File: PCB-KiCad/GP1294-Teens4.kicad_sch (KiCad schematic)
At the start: 10 parts

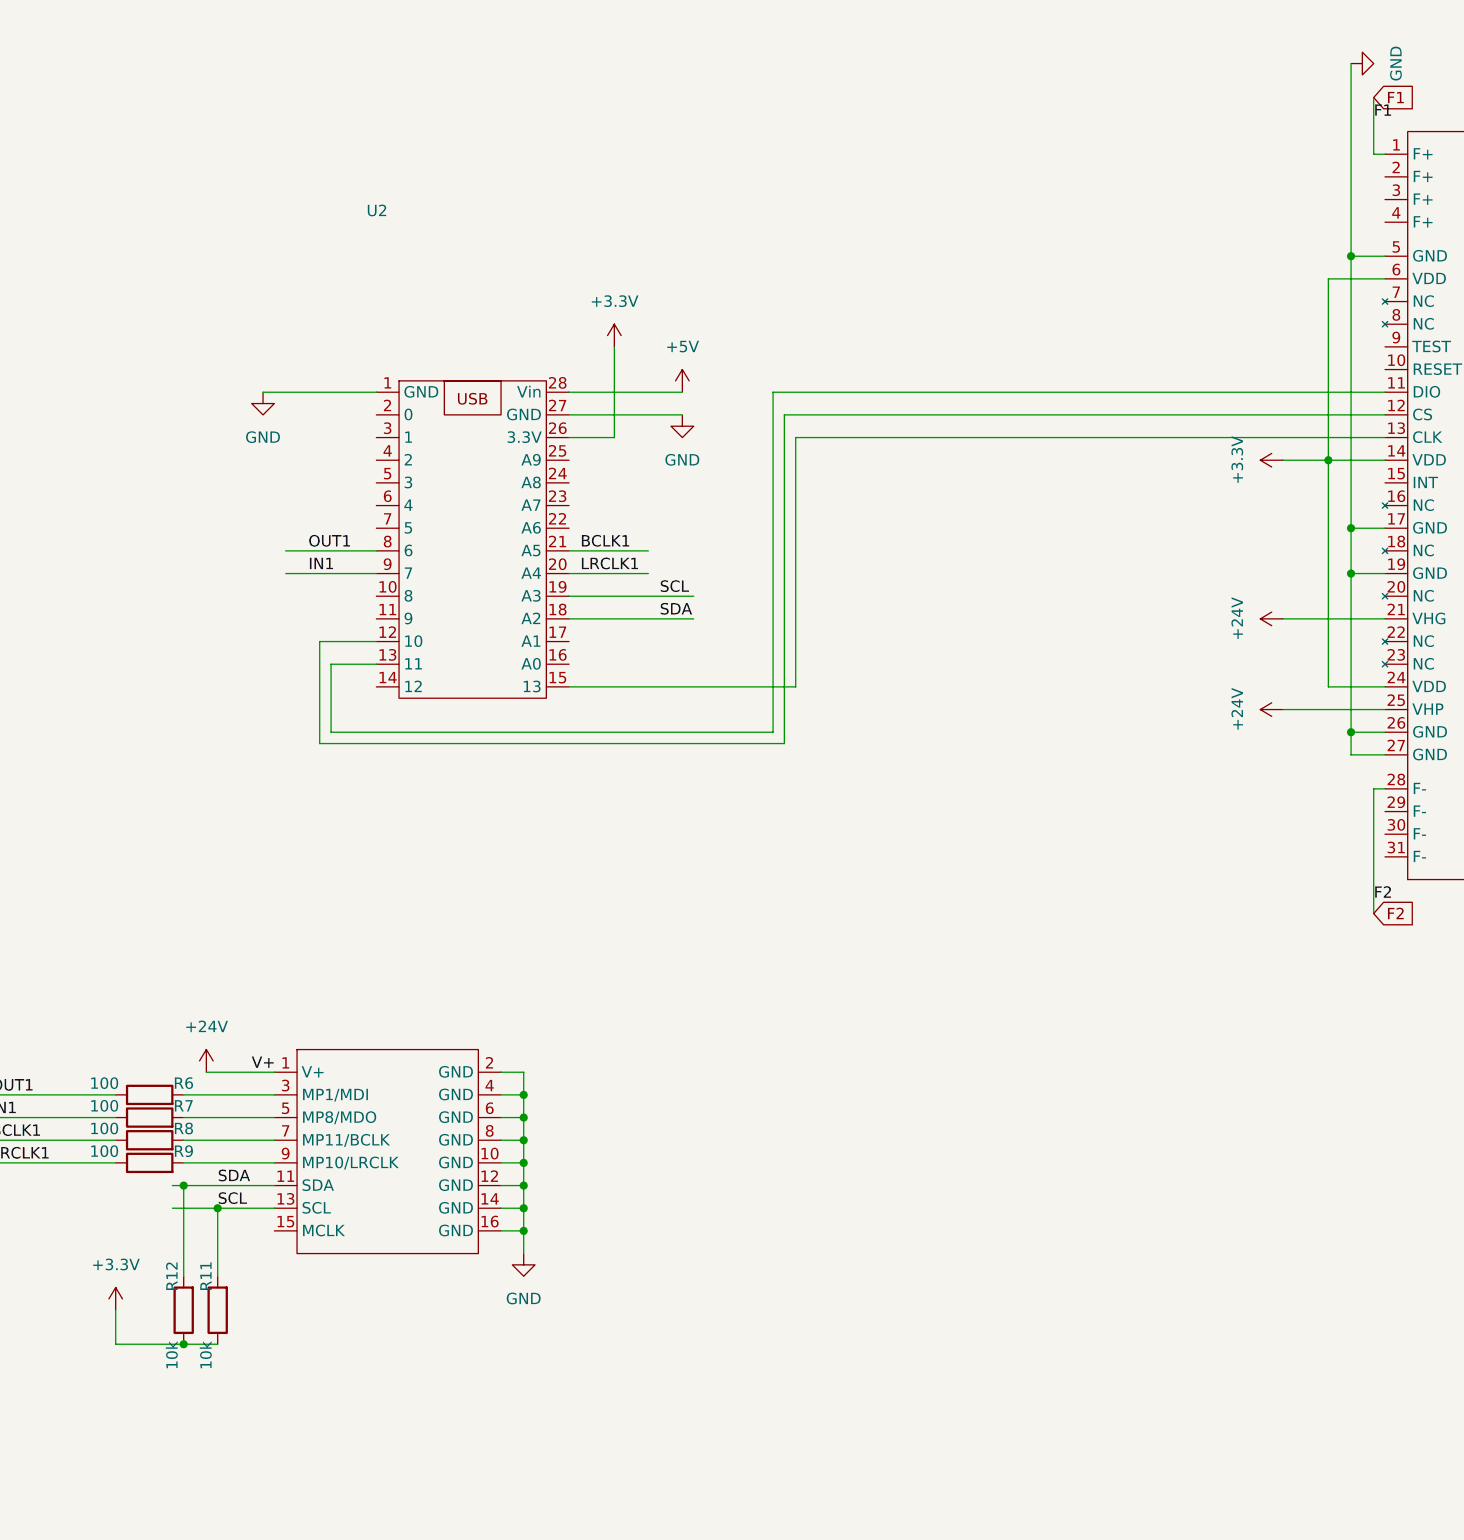
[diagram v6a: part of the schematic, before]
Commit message: GP1294 evolves
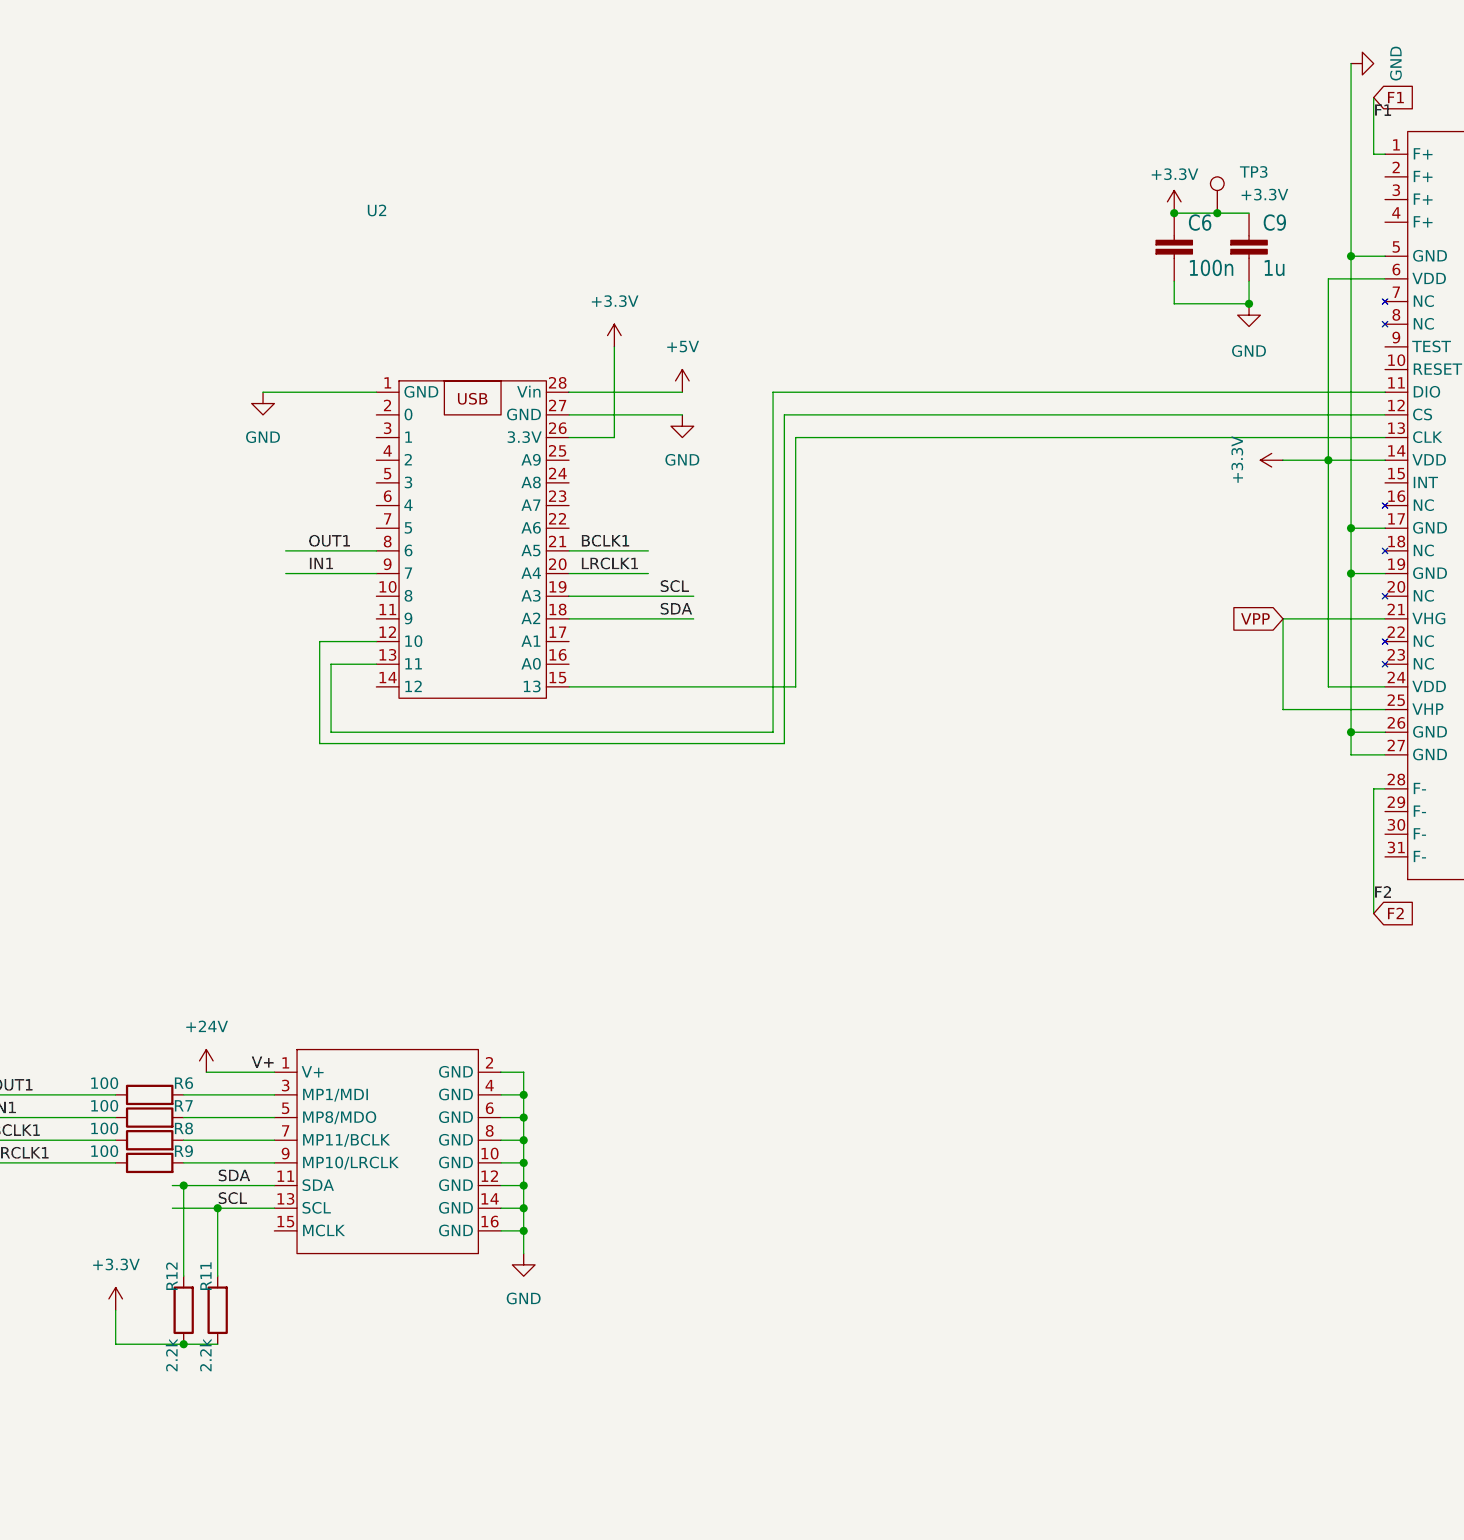
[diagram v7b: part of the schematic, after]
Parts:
- added C6: 100n, VFD-Power:C1206, symbol VFD-Power-eagle-import:C-EUC1206
- added C9: 1u, VFD-Power:C1206, symbol VFD-Power-eagle-import:C-EUC1206
- added TP3: +3.3V, TestPoint:TestPoint_Pad_2.0x2.0mm, symbol Connector:TestPoint
- R11, R12: value 10k -> 2.2k
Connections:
- net +24V: no longer U1.21 (VHG), U1.25 (VHP)
- net +3.3V: now also C6.1, C9.1, TP3.1
- net GND: now also C6.2, C9.2
- new net VPP: U1.21 (VHG), U1.25 (VHP)
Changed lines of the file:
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@@
   (junction (at 153.67 173.99) (diameter 0) (color 0 0 0 0)
   )
+  (junction (at 231.394 59.944) (diameter 0) (color 0 0 0 0)
+  )
   (junction (at 246.38 64.77) (diameter 0) (color 0 0 0 0)
   )
@@
   (junction (at 115.57 168.91) (diameter 0) (color 0 0 0 0)
   )
+  (junction (at 226.568 59.944) (diameter 0) (color 0 0 0 0)
+  )
+  (junction (at 234.95 70.104) (diameter 0) (color 0 0 0 0)
+  )
   (junction (at 153.67 163.83) (diameter 0) (color 0 0 0 0)
   )
@@
     (stroke (width 0) (type default))
   )
+  (wire (pts (xy 234.95 70.104) (xy 234.95 67.564))
+    (stroke (width 0.1524) (type solid))
+  )
+  (wire (pts (xy 231.394 59.944) (xy 226.568 59.944))
+    (stroke (width 0) (type default))
+  )
   (wire (pts (xy 153.67 158.75) (xy 153.67 161.29))
     (stroke (width 0) (type default))
@@
     (stroke (width 0) (type default))
   )
+  (wire (pts (xy 238.76 115.57) (xy 238.76 105.41))
+    (stroke (width 0) (type default))
+  )
   (wire (pts (xy 151.13 173.99) (xy 153.67 173.99))
     (stroke (width 0) (type default))
@@
     (stroke (width 0) (type default))
   )
+  (wire (pts (xy 226.568 70.104) (xy 234.95 70.104))
+    (stroke (width 0.1524) (type solid))
+  )
   (wire (pts (xy 246.38 120.65) (xy 250.19 120.65))
     (stroke (width 0) (type default))
@@
     (stroke (width 0) (type default))
   )
+  (wire (pts (xy 234.95 59.944) (xy 231.394 59.944))
+    (stroke (width 0) (type default))
+  )
   (wire (pts (xy 238.76 105.41) (xy 250.19 105.41))
     (stroke (width 0) (type default))
@@
   (wire (pts (xy 243.84 113.03) (xy 243.84 87.63))
     (stroke (width 0) (type default))
+  )
+  (wire (pts (xy 226.568 67.564) (xy 226.568 70.104))
+    (stroke (width 0.1524) (type solid))
   )
   (wire (pts (xy 153.67 168.91) (xy 153.67 171.45))
@@
     )
   )
+  (global_label "VPP" (shape input) (at 238.76 105.41 180) (fields_autoplaced)
+    (effects (font (size 1.27 1.27)) (justify right))
+    (property "Intersheetrefs" "${INTERSHEET_REFS}" (at 232.1462 105.41 0)
+      (effects (font (size 1.27 1.27)) (justify right) hide)
+    )
+  )
+  (symbol (lib_id "power:GND") (at 234.95 70.104 0) (unit 1)
+    (in_bom yes) (on_board yes) (dnp no) (fields_autoplaced)
+    (property "Reference" "#PWR04" (at 234.95 76.454 0)
+      (effects (font (size 1.27 1.27)) hide)
+    )
+    (property "Value" "GND" (at 234.95 75.438 0)
+      (effects (font (size 1.27 1.27)))
+    )
+    (property "Footprint" "" (at 234.95 70.104 0)
+      (effects (font (size 1.27 1.27)) hide)
+    )
+    (property "Datasheet" "" (at 234.95 70.104 0)
+      (effects (font (size 1.27 1.27)) hide)
+    )
+    (pin "1")
+    (instances
+      (project "GP1294-Teens4"
+        (path "/3de011e3-f89b-42a8-8637-1f4c3f0867fa"
+          (reference "#PWR04") (unit 1)
+        )
+      )
+    )
+  )
   (symbol (lib_id "power:+3.3V") (at 163.83 74.93 0) (unit 1)
     (in_bom yes) (on_board yes) (dnp no) (fields_autoplaced)
@@
     )
   )
-  (symbol (lib_id "power:+24V") (at 238.76 115.57 90) (unit 1)
-    (in_bom yes) (on_board yes) (dnp no) (fields_autoplaced)
-    (property "Reference" "#PWR03" (at 242.57 115.57 0)
-      (effects (font (size 1.27 1.27)) hide)
-    )
-    (property "Value" "+24V" (at 233.68 115.57 0)
-      (effects (font (size 1.27 1.27)))
-    )
-    (property "Footprint" "" (at 238.76 115.57 0)
-      (effects (font (size 1.27 1.27)) hide)
-    )
-    (property "Datasheet" "" (at 238.76 115.57 0)
-      (effects (font (size 1.27 1.27)) hide)
-    )
-    (pin "1")
-    (instances
-      (project "GP1294-Teens4"
-        (path "/3de011e3-f89b-42a8-8637-1f4c3f0867fa"
-          (reference "#PWR03") (unit 1)
+  (symbol (lib_id "VFD-Power-eagle-import:C-EUC1206") (at 226.568 62.484 0) (unit 1)
+    (in_bom yes) (on_board yes) (dnp no)
+    (property "Reference" "C6" (at 228.092 62.103 0)
+      (effects (font (size 1.778 1.5113)) (justify left bottom))
+    )
+    (property "Value" "100n" (at 228.092 67.183 0)
+      (effects (font (size 1.778 1.5113)) (justify left bottom))
+    )
+    (property "Footprint" "VFD-Power:C1206" (at 226.568 62.484 0)
+      (effects (font (size 1.27 1.27)) hide)
+    )
+    (property "Datasheet" "" (at 226.568 62.484 0)
+      (effects (font (size 1.27 1.27)) hide)
+    )
+    (pin "1")
+    (pin "2")
+    (instances
+      (project "GP1294-Teens4"
+        (path "/3de011e3-f89b-42a8-8637-1f4c3f0867fa"
+          (reference "C6") (unit 1)
         )
       )
@@
         (path "/3de011e3-f89b-42a8-8637-1f4c3f0867fa"
           (reference "#PWR06") (unit 1)
+        )
+      )
+    )
+  )
+  (symbol (lib_id "Connector:TestPoint") (at 231.394 59.944 0) (unit 1)
+    (in_bom yes) (on_board yes) (dnp no) (fields_autoplaced)
+    (property "Reference" "TP3" (at 233.934 55.372 0)
+      (effects (font (size 1.27 1.27)) (justify left))
+    )
+    (property "Value" "+3.3V" (at 233.934 57.912 0)
+      (effects (font (size 1.27 1.27)) (justify left))
+    )
+    (property "Footprint" "TestPoint:TestPoint_Pad_2.0x2.0mm" (at 236.474 59.944 0)
+      (effects (font (size 1.27 1.27)) hide)
+    )
+    (property "Datasheet" "~" (at 236.474 59.944 0)
+      (effects (font (size 1.27 1.27)) hide)
+    )
+    (pin "1")
+    (instances
+      (project "GP1294-Teens4"
+        (path "/3de011e3-f89b-42a8-8637-1f4c3f0867fa"
+          (reference "TP3") (unit 1)
+        )
+      )
+    )
+  )
+  (symbol (lib_id "VFD-Power-eagle-import:C-EUC1206") (at 234.95 62.484 0) (unit 1)
+    (in_bom yes) (on_board yes) (dnp no)
+    (property "Reference" "C9" (at 236.474 62.103 0)
+      (effects (font (size 1.778 1.5113)) (justify left bottom))
+    )
+    (property "Value" "1u" (at 236.474 67.183 0)
+      (effects (font (size 1.778 1.5113)) (justify left bottom))
+    )
+    (property "Footprint" "VFD-Power:C1206" (at 234.95 62.484 0)
+      (effects (font (size 1.27 1.27)) hide)
+    )
+    (property "Datasheet" "" (at 234.95 62.484 0)
+      (effects (font (size 1.27 1.27)) hide)
+    )
+    (pin "1")
+    (pin "2")
+    (instances
+      (project "GP1294-Teens4"
+        (path "/3de011e3-f89b-42a8-8637-1f4c3f0867fa"
+          (reference "C9") (unit 1)
         )
       )
@@
       (effects (font (size 1.27 1.27)))
     )
-    (property "Value" "10k" (at 114.3 187.96 90)
+    (property "Value" "2.2k" (at 114.3 187.96 90)
       (effects (font (size 1.27 1.27)))
     )
@@
     )
   )
-  (symbol (lib_id "power:+24V") (at 238.76 105.41 90) (unit 1)
-    (in_bom yes) (on_board yes) (dnp no) (fields_autoplaced)
-    (property "Reference" "#PWR04" (at 242.57 105.41 0)
-      (effects (font (size 1.27 1.27)) hide)
-    )
-    (property "Value" "+24V" (at 233.68 105.41 0)
-      (effects (font (size 1.27 1.27)))
-    )
-    (property "Footprint" "" (at 238.76 105.41 0)
-      (effects (font (size 1.27 1.27)) hide)
-    )
-    (property "Datasheet" "" (at 238.76 105.41 0)
-      (effects (font (size 1.27 1.27)) hide)
-    )
-    (pin "1")
-    (instances
-      (project "GP1294-Teens4"
-        (path "/3de011e3-f89b-42a8-8637-1f4c3f0867fa"
-          (reference "#PWR04") (unit 1)
+  (symbol (lib_id "power:+3.3V") (at 226.568 59.944 0) (unit 1)
+    (in_bom yes) (on_board yes) (dnp no) (fields_autoplaced)
+    (property "Reference" "#PWR03" (at 226.568 63.754 0)
+      (effects (font (size 1.27 1.27)) hide)
+    )
+    (property "Value" "+3.3V" (at 226.568 55.626 0)
+      (effects (font (size 1.27 1.27)))
+    )
+    (property "Footprint" "" (at 226.568 59.944 0)
+      (effects (font (size 1.27 1.27)) hide)
+    )
+    (property "Datasheet" "" (at 226.568 59.944 0)
+      (effects (font (size 1.27 1.27)) hide)
+    )
+    (pin "1")
+    (instances
+      (project "GP1294-Teens4"
+        (path "/3de011e3-f89b-42a8-8637-1f4c3f0867fa"
+          (reference "#PWR03") (unit 1)
         )
       )
@@
       (effects (font (size 1.27 1.27)))
     )
-    (property "Value" "10k" (at 118.11 187.96 90)
+    (property "Value" "2.2k" (at 118.11 187.96 90)
       (effects (font (size 1.27 1.27)))
     )
@@
       (effects (font (size 1.27 1.27)) hide)
     )
+    (property "Field4" "" (at 119.38 182.88 90)
+      (effects (font (size 1.27 1.27)) hide)
+    )

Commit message: Added SRC.
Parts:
- removed R6: 100, Resistor_SMD:R_0603_1608Metric, symbol Device:R
- added U8: CS8421, VFDs-Library:CS8421-breakout, symbol VFDs-Library:CS8421-breakout
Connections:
- net +3.3V: now also U8.10 (3.3-5V), U8.2 (3.3-5V)
- net BCLK1: now also U8.8 (BCK_IN); no longer R8.1
- net GND: now also U8.1 (GND), U8.11 (GND)
- net IN1: no longer R7.1
- net LRCLK1: now also U8.9 (LRCK_IN); no longer R9.1
- net OUT1: now also U8.7 (DATA_IN)
- new net BCK_OUT: R8.1, U8.4 (BCK_OUT)
- new net DATA_OUT: R7.1, U8.5 (DATA_OUT)
- new net LRCK_OUT: R9.1, U8.3 (LRCK_OUT)
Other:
- note added: "CS8421 I2S IIS Sampling Rate Conversion Module Configure as SlaveIn SlaveOut ! MSEL pin 15 -> 1k to GND SAIF pin 19 -> 1k to GND (input i2s anything) SAOF pin 18 -> 4k to GND (output i2s 24bit)"
